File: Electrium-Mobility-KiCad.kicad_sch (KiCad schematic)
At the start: 13 parts, among them M1 3V 75mA, SW1 SW_Push, SW2 SW_Push, U1 ESP32-WROOM-32E, U2 LCD-016N002L

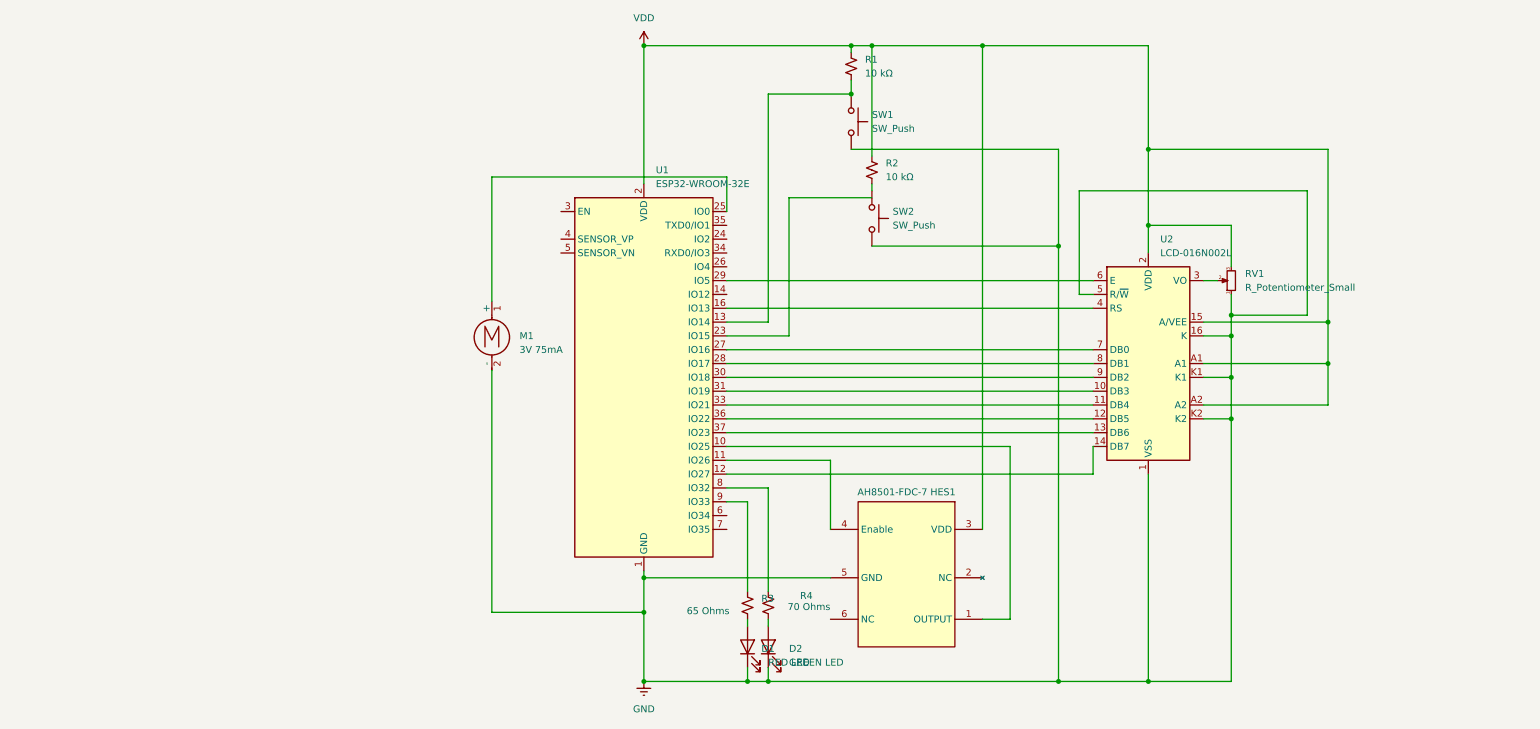
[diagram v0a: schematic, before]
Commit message: Battery charger circuit
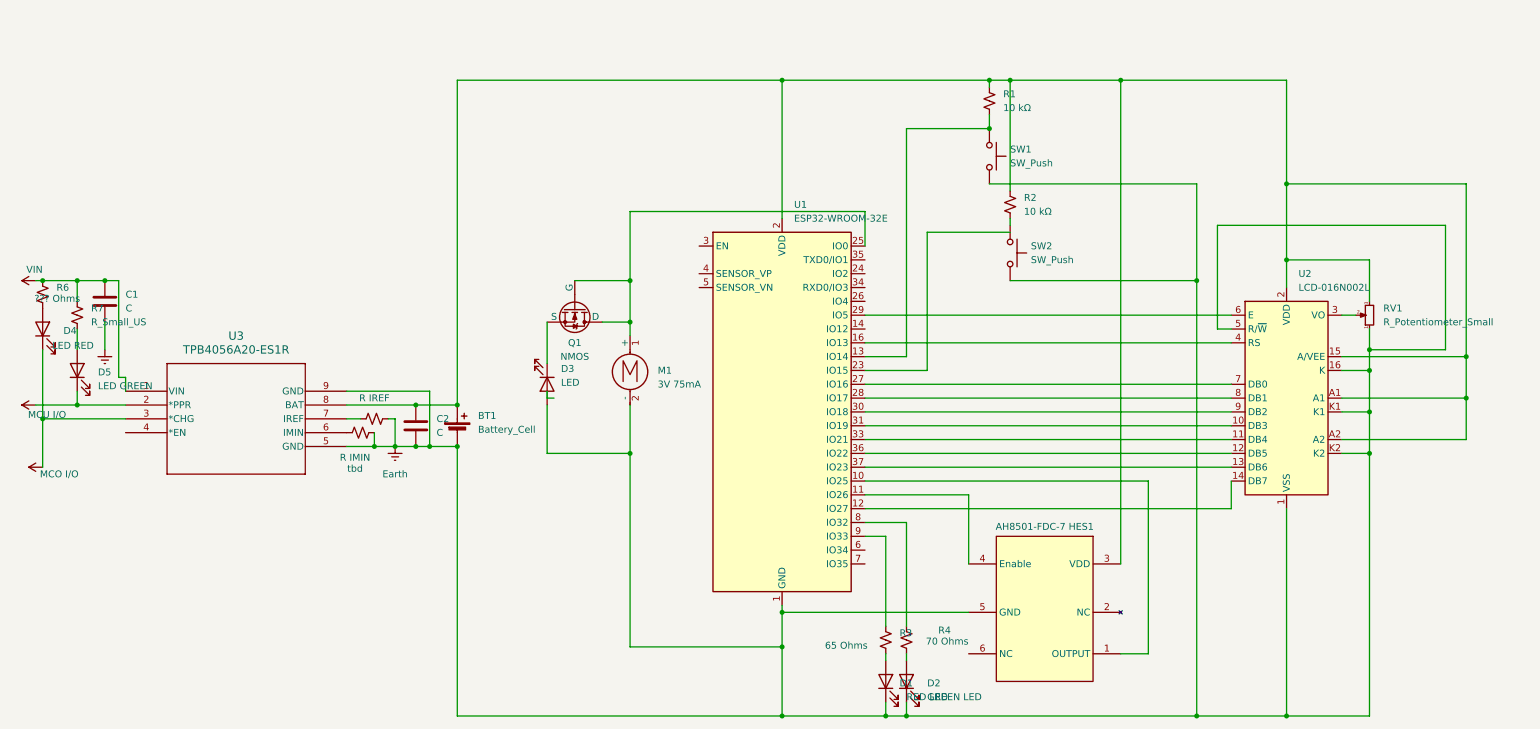
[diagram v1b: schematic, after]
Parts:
- added BT1: Battery_Cell, symbol Device:Battery_Cell
- added C1, C2: C, symbol Device:C
- added D3: LED, symbol Device:LED
- added D4: LED RED, symbol Device:LED
- added D5: LED GREEN, symbol Device:LED
- added Q1: NMOS, symbol Simulation_SPICE:NMOS
- added R IMIN: tbd, symbol Device:R_Small_US
- added R IREF: ~, symbol Device:R_Small_US
- added R6: ??? Ohms, symbol Device:R_Small_US
- added R7: R_Small_US, symbol Device:R_Small_US
- added U3: TPB4056A20-ES1R, ESOP-8_TPK, symbol 2024-11-20_13-12-45:TPB4056A20-ES1R
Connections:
- net at M1.1 (+), U1.25 (IO0): now also Q1.1 (D), Q1.2 (G)
- net GND renamed Earth
- net Earth: now also BT1.2 (-), C2.2, D3.2 (A), R IMIN.2, R IREF.2, U3.5 (GND), U3.9 (GND)
- net VDD: no longer names the net of AH8501-FDC-7 HES1.3 (VDD), R1.1, R2.1, RV1.3, U1.2 (VDD), U2.15 (A/VEE), U2.2 (VDD), U2.A1, U2.A2
- net VDD: now also BT1.1 (+), C2.1, U3.8 (BAT)
- new net: D4.2 (A), R6.2
- new net: R IMIN.1, U3.6 (IMIN)
- new net: R IREF.1, U3.7 (IREF)
- new net: D5.2 (A), R7.2
- new net: D3.1 (K), Q1.3 (S)
- new net MCO I/O: D4.1 (K), U3.3 (*CHG)
- new net MCU I/O: D5.1 (K), U3.2 (*PPR)
- new net VIN: C1.1, R6.1, R7.1, U3.1 (VIN)
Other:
- moved on the sheet: AH8501-FDC-7 HES1, D1, D2, M1, R1, R2, R3, R4, RV1, SW1, SW2, U1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
